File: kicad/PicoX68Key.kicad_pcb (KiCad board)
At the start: 2 copper layers, 33.9 x 69 mm, 20 parts, among them J1 TO_X68000, Q1 2N7000, Q1 2N7002, Q2 2N7000, Q2 2N7002, Q3 2N7000, Q3 2N7002, U1 Pico

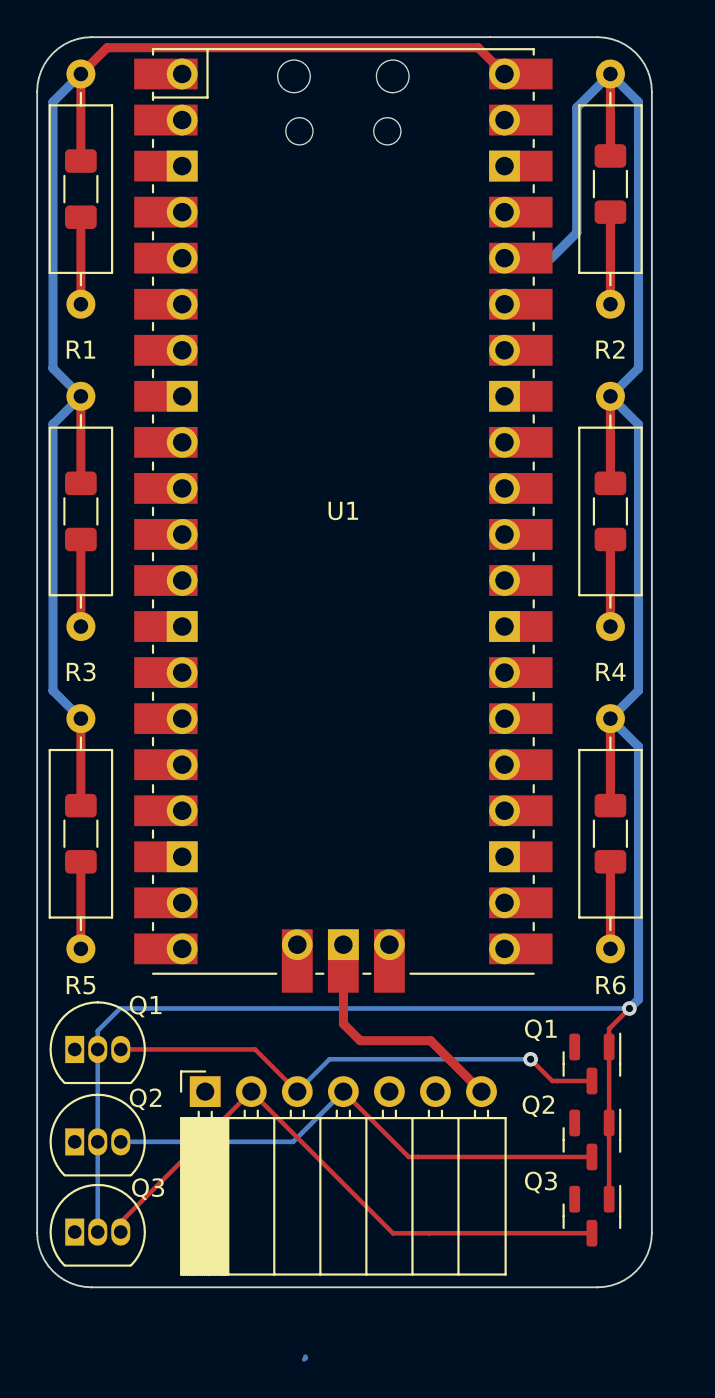
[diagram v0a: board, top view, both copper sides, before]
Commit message: Add mini-din7 connector, finish routing
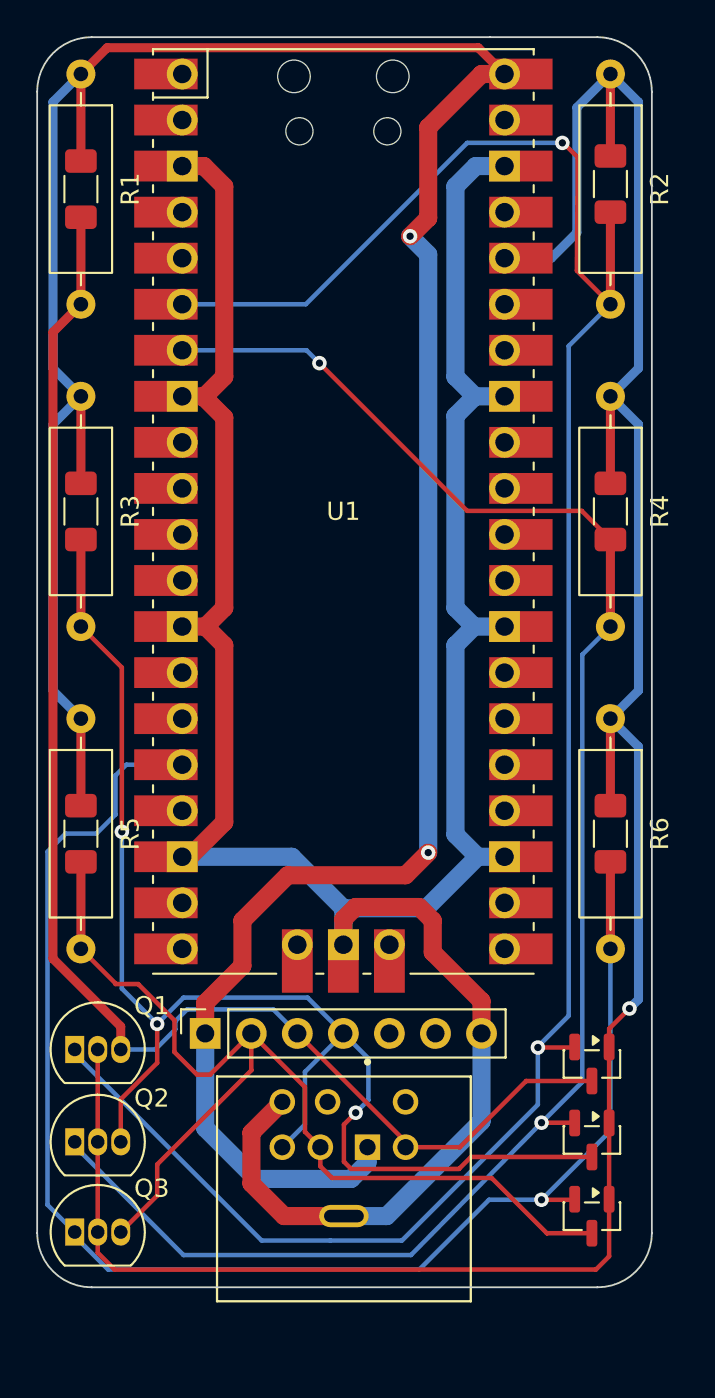
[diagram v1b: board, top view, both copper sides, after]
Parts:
- added J2: MD-70S, Library:CUI_MD-70S, F.Cu at (83.8, 145.6)
- J1: footprint Library:PinSocket_1x07_P2.54mm_Horizontal -> Library:PinSocket_1x07_P2.54mm_Vertical
- moved J1 3.21 mm to (76.2, 135.5)
- renumbered Q1 to SQ1, Q2 to SQ2, Q3 to SQ3
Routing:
- net GND: track 13.5 -> 153.1 mm
- net KB_TX_L: track 5.08 -> 120.8 mm, vias 0 -> 2
- net KB_RX_L: track 4.80 -> 95.1 mm, vias 0 -> 2
- net VBUS: track 77.1 -> 158.8 mm, vias 0 -> 2
- net MS_TX_L: track 4.80 -> 82.7 mm, vias 0 -> 1
- net KB_TX_H: track 33.0 -> 80.1 mm, vias 1 -> 0
- net KB_RX_H: track 33.4 -> 77.5 mm, vias 0 -> 3
- net MS_TX_H: track 37.6 -> 59.0 mm
- net 3V3: track 135.1 -> 137.4 mm

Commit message: Layout tidy up, add flood planes
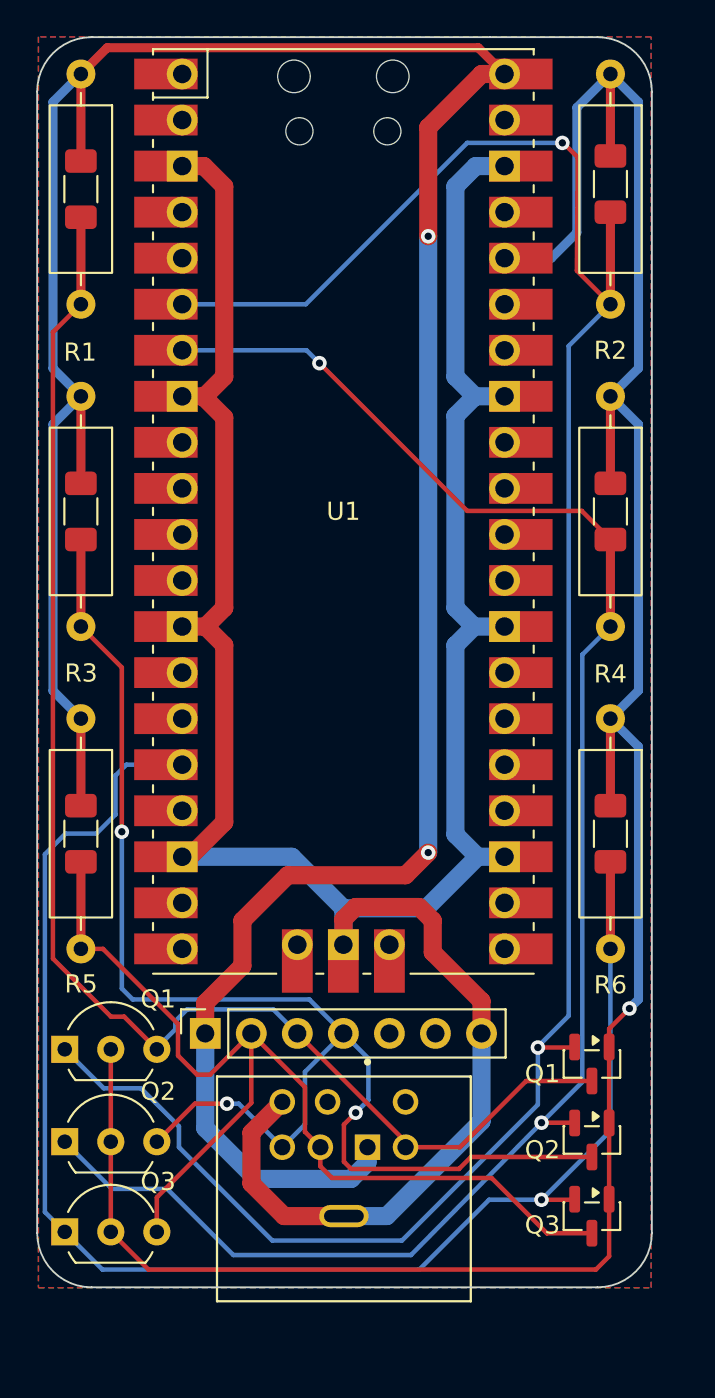
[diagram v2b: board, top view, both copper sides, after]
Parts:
- J1: footprint Library:PinSocket_1x07_P2.54mm_Vertical -> Connector_PinSocket_2.54mm:PinSocket_1x07_P2.54mm_Vertical
- Q1, Q2, Q3: footprint Library:TO-92_Inline -> Package_TO_SOT_THT:TO-92L_Inline_Wide
- R1, R2, R3, R4, R5, R6: footprint Library:R_Axial_DIN0309_L9.0mm_D3.2mm_P12.70mm_Horizontal -> Resistor_THT:R_Axial_DIN0309_L9.0mm_D3.2mm_P12.70mm_Horizontal
- R10, R11, R12, R7, R8, R9: footprint Library:R_1206_3216Metric_Pad1.30x1.75mm_HandSolder -> Resistor_SMD:R_1206_3216Metric_Pad1.30x1.75mm_HandSolder
- SQ1, SQ2, SQ3: footprint Library:SOT-23 -> Package_TO_SOT_SMD:SOT-23
- U1: footprint Library:RPi_Pico_SMD_TH -> MCU_RaspberryPi_and_Boards:RPi_Pico_SMD_TH
- moved Q1 0.55 mm to (68.5, 136.3)
- moved Q3 0.55 mm to (68.5, 146.4)
- moved Q2 0.55 mm to (68.5, 141.4)
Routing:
- net MS_TX_H: track 59.0 -> 57.6 mm
- net 3V3: track 137.4 -> 136.0 mm
- net KB_TX_L: track 120.8 -> 122.1 mm
- net MS_TX_L: track 82.7 -> 83.5 mm
- net VBUS: track 158.8 -> 158.0 mm
- net KB_TX_H: track 80.1 -> 79.4 mm
- net KB_RX_L: track 95.1 -> 95.7 mm
- added copper zone on B.Cu, net 3V3
- added copper zone on F.Cu, net GND
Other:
- board text added: "Q1"
- board text added: "Q2"
- board text added: "Q3"

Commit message: New Pico footprint, change pin header to be SPI for future LED board
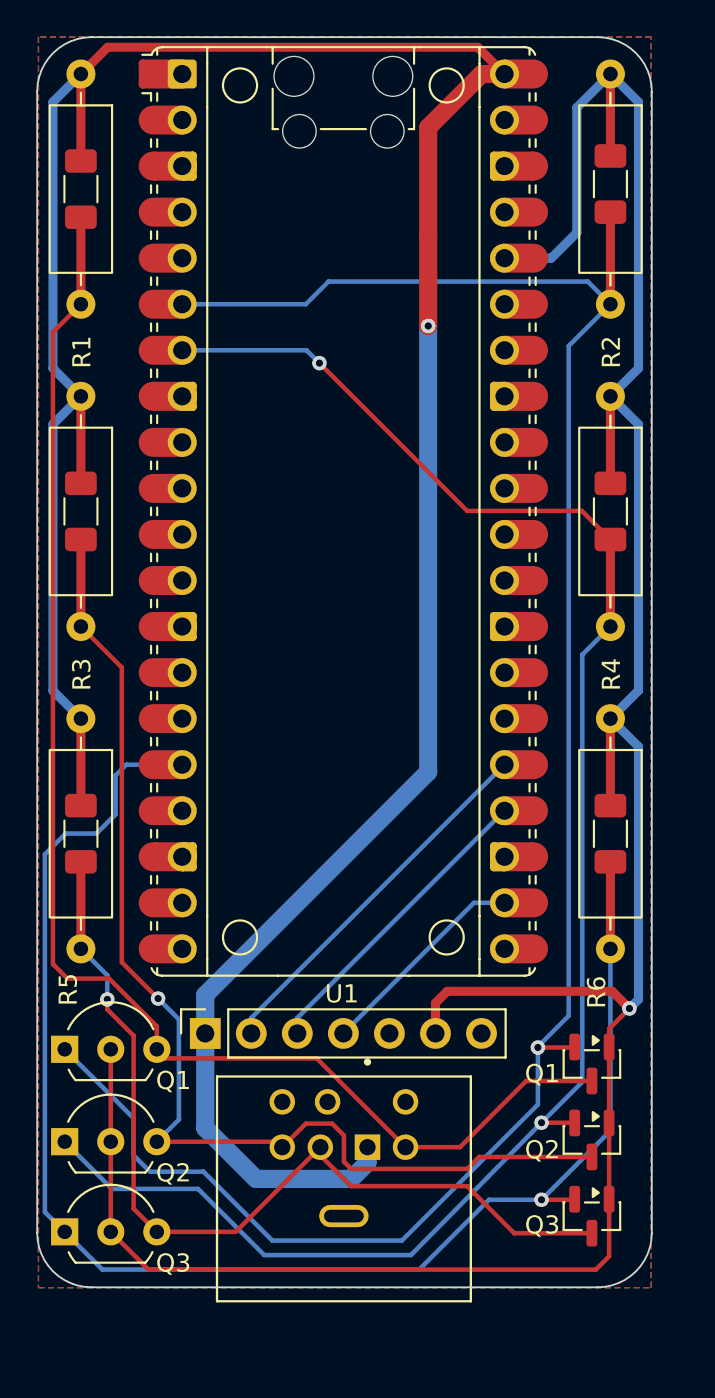
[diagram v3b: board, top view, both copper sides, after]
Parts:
- J1: value TO_X68000 -> LED_BOARD; footprint Connector_PinSocket_2.54mm:PinSocket_1x07_P2.54mm_Vertical -> Library:PinSocket_1x07_P2.54mm_Vertical
- Q1, Q2, Q3: footprint Package_TO_SOT_THT:TO-92L_Inline_Wide -> Library:TO-92L_Inline_Wide
- R1, R2, R3, R4, R5, R6: footprint Resistor_THT:R_Axial_DIN0309_L9.0mm_D3.2mm_P12.70mm_Horizontal -> Library:R_Axial_DIN0309_L9.0mm_D3.2mm_P12.70mm_Horizontal
- R10, R11, R12, R7, R8, R9: footprint Resistor_SMD:R_1206_3216Metric_Pad1.30x1.75mm_HandSolder -> Library:R_1206_3216Metric_Pad1.30x1.75mm_HandSolder
- SQ1, SQ2, SQ3: footprint Package_TO_SOT_SMD:SOT-23 -> Library:SOT-23
- U1: footprint MCU_RaspberryPi_and_Boards:RPi_Pico_SMD_TH -> Library:RaspberryPi_Pico_Common
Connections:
- J1 pad 2: MS_TX_H -> MOSI
- J1 pad 3: KB_TX_H -> SCL
- J1 pad 4: KB_RX_H -> CS
- J1 pad 6: unconnected-(J1-Pin_6-Pad6) -> 3V3
- U1 pad 22: unconnected-(U1-GPIO17-Pad22) -> CS
- U1 pad 24: unconnected-(U1-GPIO18-Pad24) -> SCL
- U1 pad 25: unconnected-(U1-GPIO19-Pad25) -> MOSI
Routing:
- net GND: track 153.1 -> 0.00 mm
- net MOSI: track 0.00 -> 20.6 mm
- net SCL: track 0.00 -> 17.0 mm
- net KB_RX_H: track 77.7 -> 62.8 mm, vias 3 -> 1
- net 3V3: track 136.0 -> 149.1 mm
- net CS: track 0.00 -> 11.9 mm
- net KB_TX_L: track 122.1 -> 112.6 mm, vias 2 -> 1
- net MS_TX_H: track 57.6 -> 50.3 mm, vias 0 -> 1
- net VBUS: track 158.0 -> 154.2 mm, vias 2 -> 1
- net KB_TX_H: track 79.4 -> 78.0 mm
- added copper zone on B.Cu, net GND
- removed copper zone on B.Cu, net 3V3
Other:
- board text added: "0V"
- board text added: "3.3V"
- board text added: "5V"
- board text added: "CS"
- board text added: "MOSI"
- board text added: "SCL"
- board text added: "SPI0"
